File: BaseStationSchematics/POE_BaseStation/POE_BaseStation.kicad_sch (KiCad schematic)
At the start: 3 parts, among them J1 Conn_01x10_Socket, J2 Conn_01x10_Socket, U1 Ra01_Breakout_Module-Ra01_Bre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

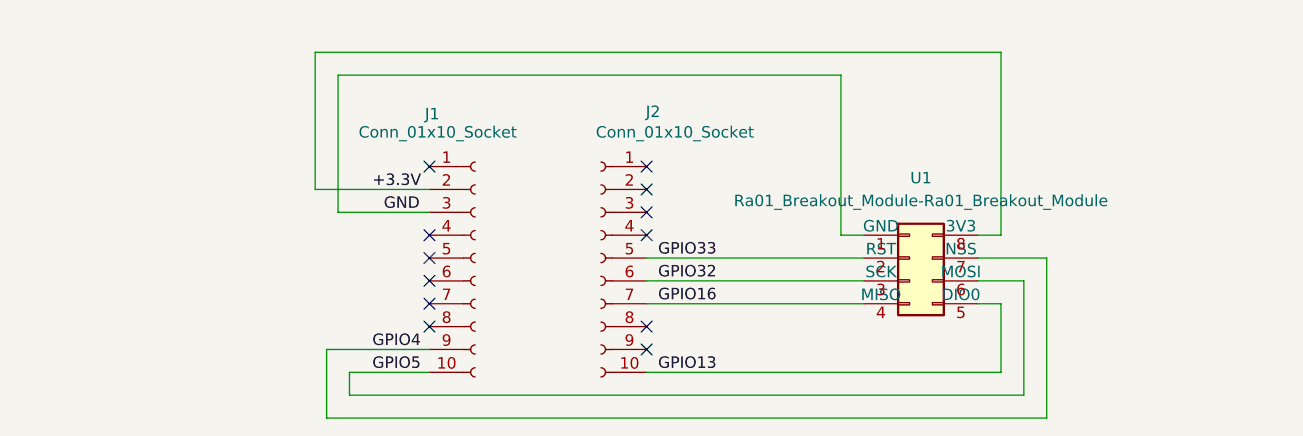
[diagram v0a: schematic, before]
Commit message: Made speaker and external LEDs optional, pins defined in platformio.ini
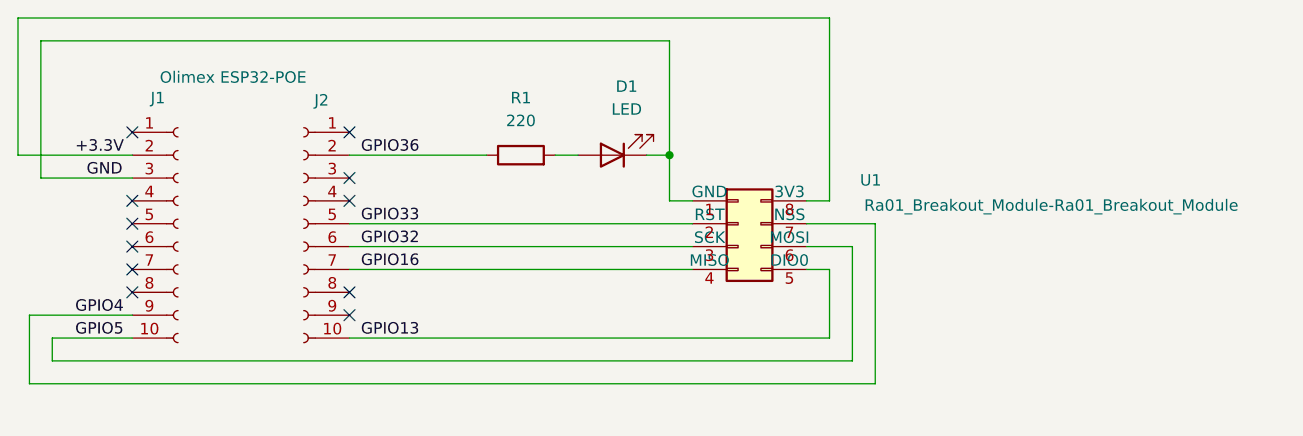
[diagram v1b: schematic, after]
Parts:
- added D1: LED, symbol Device:LED
- added R1: 220, symbol Device:R
- J1: value Conn_01x10_Socket -> Olimex ESP32-POE
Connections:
- net GND: now also D1.1 (K)
- net GPIO36: now reaches J2.2 (Pin_2)
- net GPIO36: now also R1.1
- new net: D1.2 (A), R1.2
- no-connect marks 12 -> 11
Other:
- company: (none) -> Jotham Gates
- title: (none) -> Farm monitor gateway - POE version
- moved on the sheet: J1, J2, U1

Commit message: Schematic and board layout matches POE, started adding ethernet support
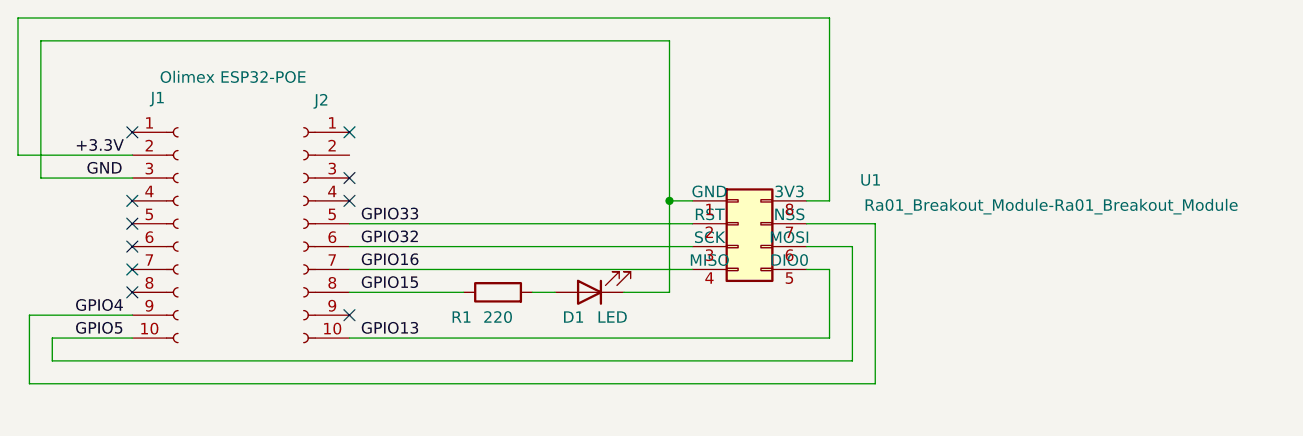
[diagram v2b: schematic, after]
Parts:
- D1: footprint (none) -> LED_THT:LED_D3.0mm
- R1: footprint (none) -> Resistor_THT:R_Axial_DIN0207_L6.3mm_D2.5mm_P15.24mm_Horizontal
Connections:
- net GPIO15: now reaches J2.8 (Pin_8)
- net GPIO15: now also R1.1
- net GPIO36: no longer names the net of J2.2 (Pin_2)
- net GPIO36: no longer R1.1
- no-connect marks 11 -> 10
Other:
- moved on the sheet: D1, R1
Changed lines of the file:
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@@
 	)
 	(junction
-		(at 162.56 88.9)
+		(at 162.56 93.98)
 		(diameter 0)
 		(color 0 0 0 0)
 	)
 	(no_connect
-		(at 127 104.14)
-	)
-	(no_connect
 		(at 127 86.36)
 	)
@@
 	(wire
 		(pts
-			(xy 160.02 88.9) (xy 162.56 88.9)
+			(xy 157.48 104.14) (xy 162.56 104.14)
 		)
 		(stroke
@@
 	(wire
 		(pts
-			(xy 149.86 88.9) (xy 152.4 88.9)
-		)
-		(stroke
-			(width 0)
-			(type default)
-		)
-	)
-	(wire
-		(pts
-			(xy 127 88.9) (xy 142.24 88.9)
+			(xy 147.32 104.14) (xy 149.86 104.14)
+		)
+		(stroke
+			(width 0)
+			(type default)
+		)
+	)
+	(wire
+		(pts
+			(xy 127 104.14) (xy 139.7 104.14)
 		)
 		(stroke
@@
 	(wire
 		(pts
-			(xy 162.56 88.9) (xy 162.56 76.2)
+			(xy 162.56 76.2) (xy 162.56 93.98)
 		)
 		(stroke
@@
 	(wire
 		(pts
-			(xy 162.56 93.98) (xy 162.56 88.9)
+			(xy 162.56 93.98) (xy 162.56 104.14)
 		)
 		(stroke
@@
 		)
 	)
-	(label "GPIO36"
-		(at 128.27 88.9 0)
+	(label "GPIO15"
+		(at 128.27 104.14 0)
 		(fields_autoplaced yes)
 		(effects
@@
 	(symbol
 		(lib_id "Device:R")
-		(at 146.05 88.9 90)
+		(at 143.51 104.14 90)
 		(unit 1)
 		(exclude_from_sim no)
@@
 		(on_board yes)
 		(dnp no)
-		(fields_autoplaced yes)
 		(property "Reference" "R1"
-			(at 146.05 82.55 90)
+			(at 139.446 106.934 90)
 			(effects
 				(font
@@
 		)
 		(property "Value" "220"
-			(at 146.05 85.09 90)
-			(effects
-				(font
-					(size 1.27 1.27)
-				)
-			)
-		)
-		(property "Footprint" ""
-			(at 146.05 90.678 90)
+			(at 143.51 106.934 90)
+			(effects
+				(font
+					(size 1.27 1.27)
+				)
+			)
+		)
+		(property "Footprint" "Resistor_THT:R_Axial_DIN0207_L6.3mm_D2.5mm_P15.24mm_Horizontal"
+			(at 143.51 105.918 90)
 			(effects
 				(font
@@
 		)
 		(property "Datasheet" "~"
-			(at 146.05 88.9 0)
+			(at 143.51 104.14 0)
 			(effects
 				(font
@@
 		)
 		(property "Description" "Resistor"
-			(at 146.05 88.9 0)
+			(at 143.51 104.14 0)
 			(effects
 				(font
@@
 	(symbol
 		(lib_id "Device:LED")
-		(at 156.21 88.9 180)
+		(at 153.67 104.14 180)
 		(unit 1)
 		(exclude_from_sim no)
@@
 		(on_board yes)
 		(dnp no)
-		(fields_autoplaced yes)
 		(property "Reference" "D1"
-			(at 157.7975 81.28 0)
+			(at 151.892 106.934 0)
 			(effects
 				(font
@@
 		)
 		(property "Value" "LED"
-			(at 157.7975 83.82 0)
-			(effects
-				(font
-					(size 1.27 1.27)
-				)
-			)
-		)
-		(property "Footprint" ""
-			(at 156.21 88.9 0)
+			(at 156.21 106.934 0)
+			(effects
+				(font
+					(size 1.27 1.27)
+				)
+			)
+		)
+		(property "Footprint" "LED_THT:LED_D3.0mm"
+			(at 153.67 104.14 0)
 			(effects
 				(font
@@
 		)
 		(property "Datasheet" "~"
-			(at 156.21 88.9 0)
+			(at 153.67 104.14 0)
 			(effects
 				(font
@@
 		)
 		(property "Description" "Light emitting diode"
-			(at 156.21 88.9 0)
-			(effects
-				(font
+			(at 153.67 104.14 0)
+			(effects
+				(font
